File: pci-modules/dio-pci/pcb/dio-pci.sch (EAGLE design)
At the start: 132 parts, among them IC1 AZ1117CH-3.3, Q1 BSH103, Q2 BSH103, U1 4901, U3 ADN4663, U4 ADN4663, U5 ADN4664, U6 MEV3S1209SC, U7 4901

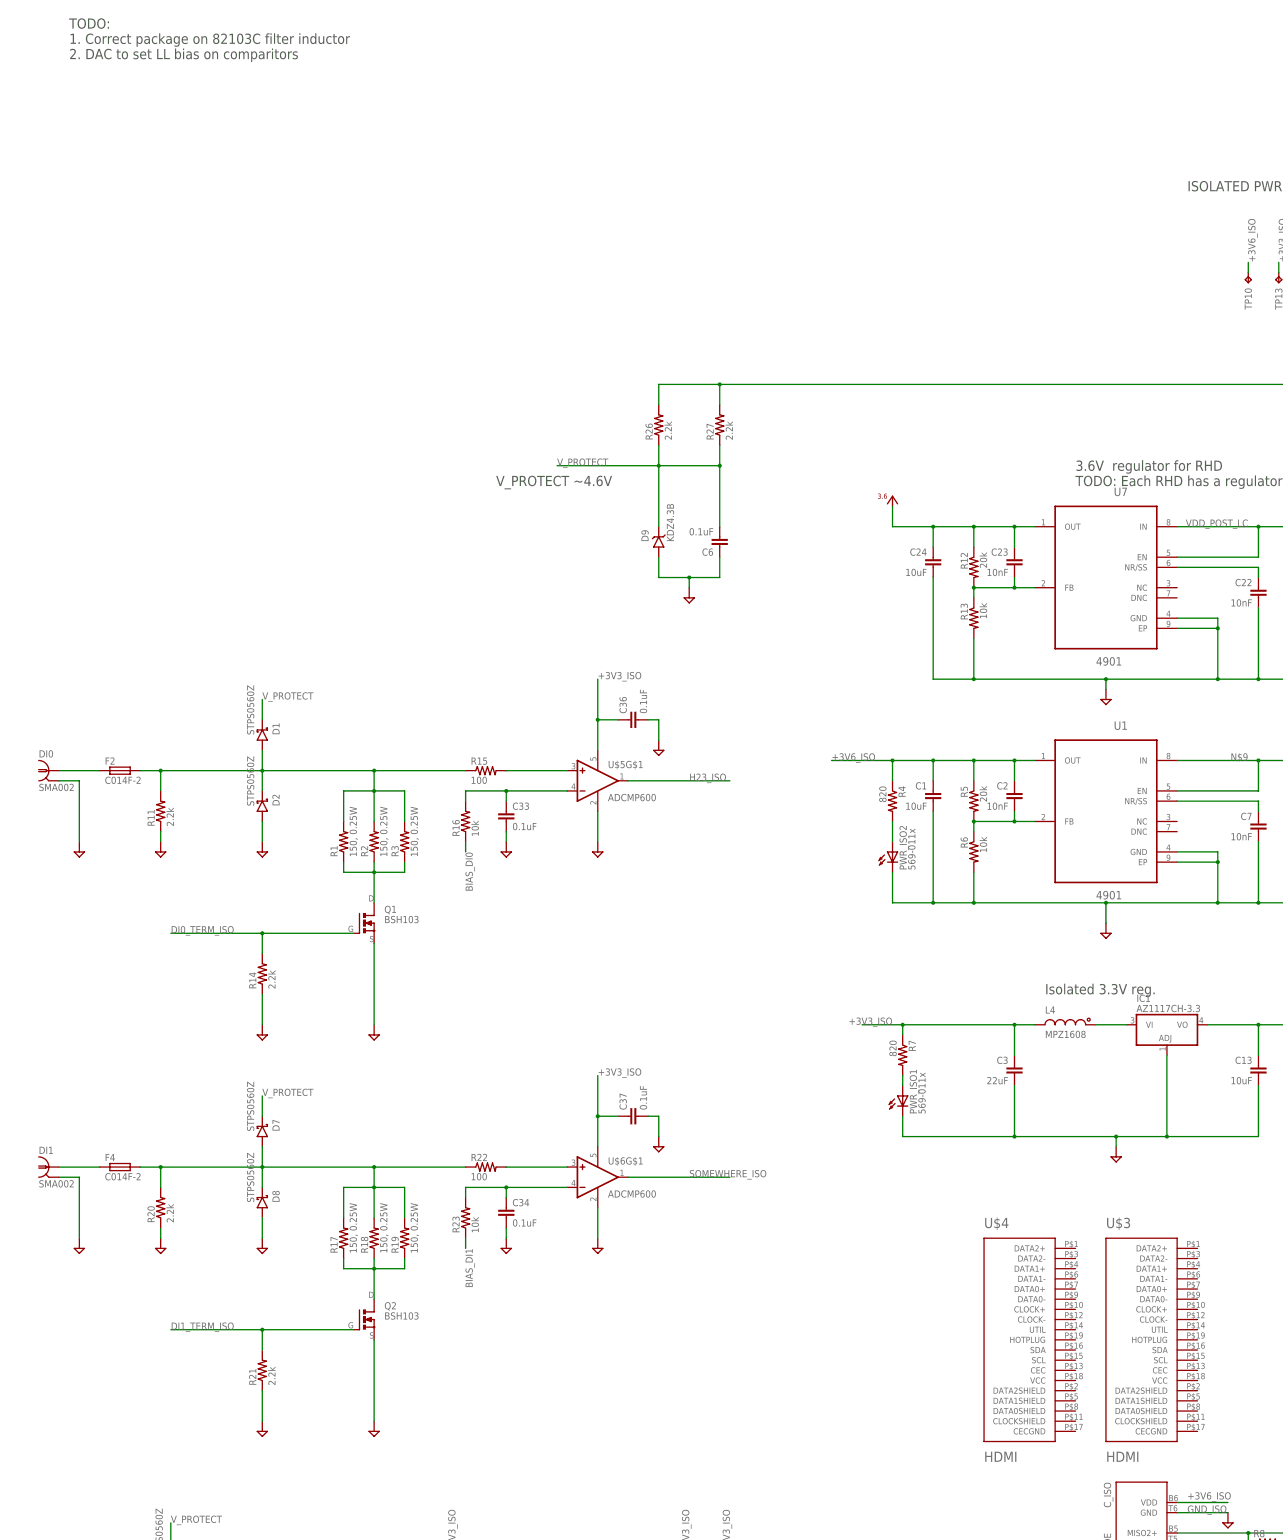
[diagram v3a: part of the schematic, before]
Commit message: Added some design ideas to dio-pci README.
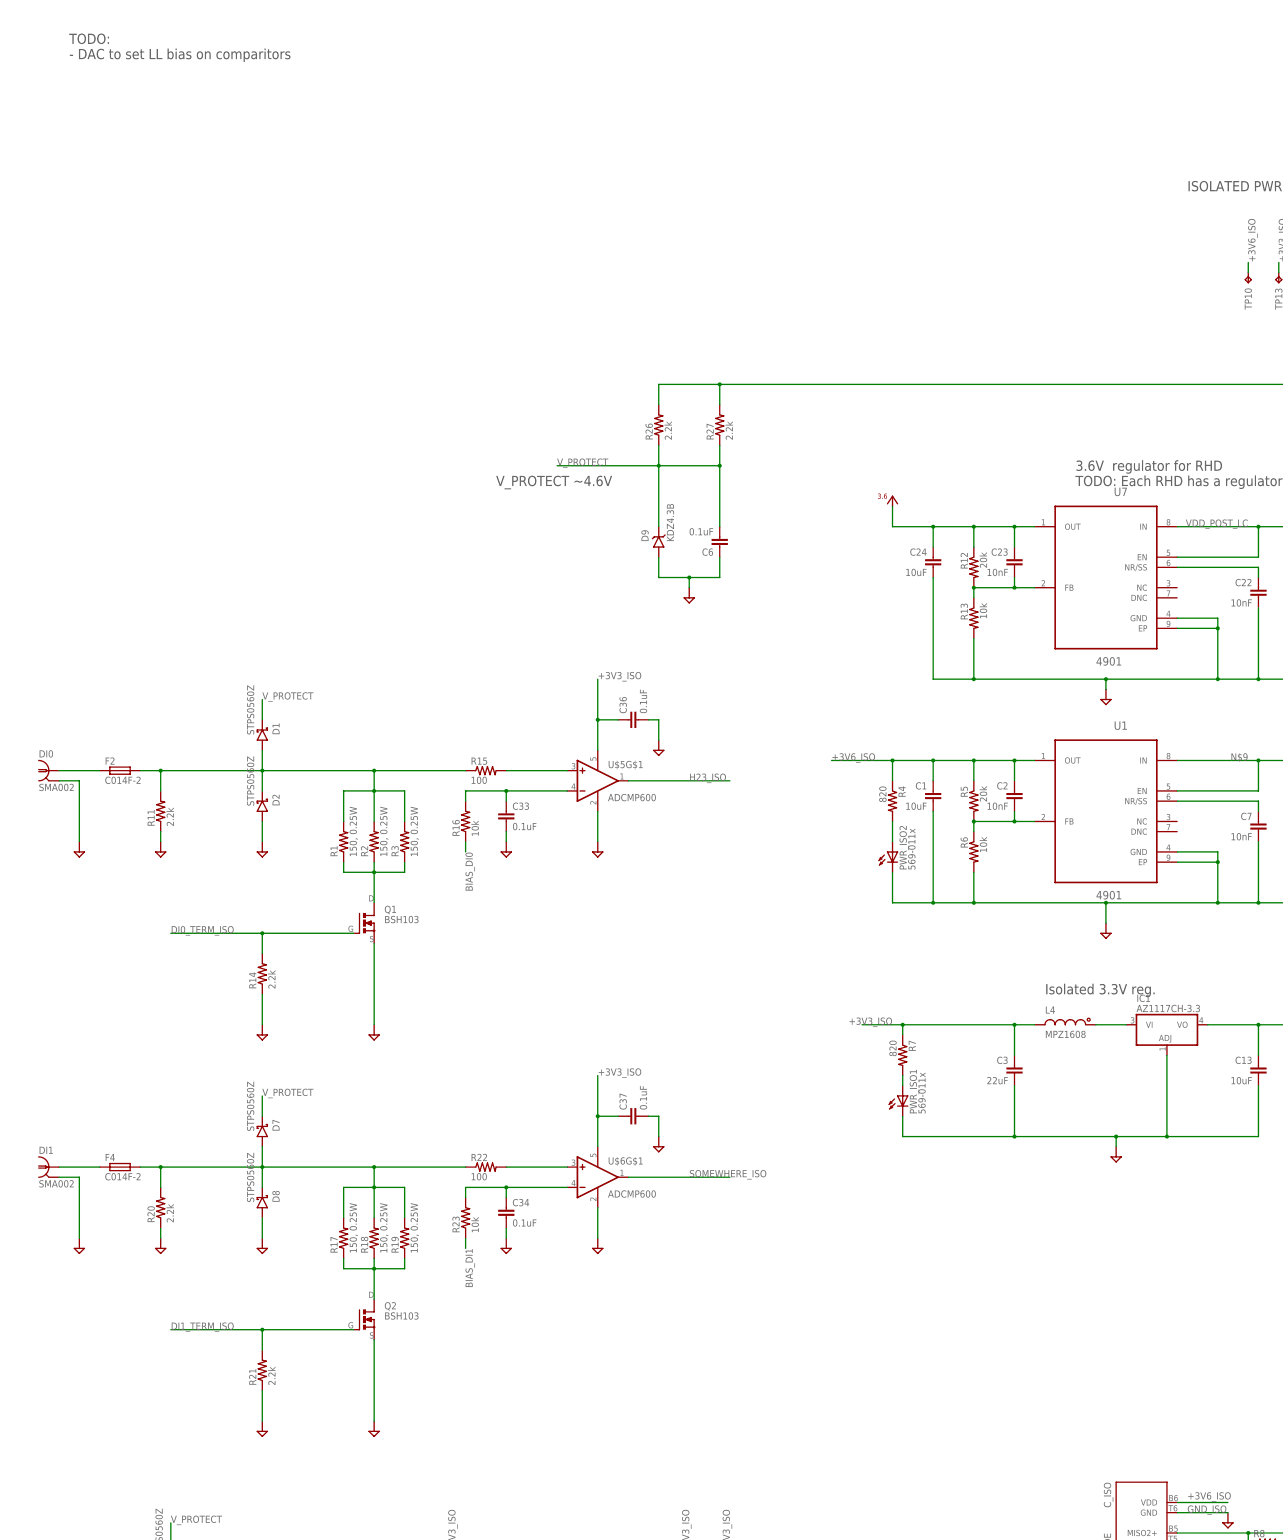
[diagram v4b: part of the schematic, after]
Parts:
- removed U$3, U$4: HDMI, jonnew:HDMI
- L5: device jonnew:L_1206 -> jonnew:L_1210
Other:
- note added: "TODO: - DAC to set LL bias on comparitors"
- note removed: "TODO: 1. Correct package on 82103C filter inductor 2. DAC to set LL bias on comparitors"
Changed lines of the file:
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@@
 <setting verticaltext="up"/>
 </settings>
-<grid distance="0.1" unitdist="inch" unit="inch" style="lines" multiple="1" display="yes" altdistance="0.01" altunitdist="inch" altunit="inch"/>
+<grid distance="0.1" unitdist="inch" unit="inch" style="lines" multiple="1" display="no" altdistance="0.01" altunitdist="inch" altunit="inch"/>
 <layers>
 <layer number="1" name="Top" color="4" fill="1" visible="no" active="no"/>
@@
 <layer number="91" name="Nets" color="2" fill="1" visible="yes" active="yes"/>
 <layer number="92" name="Busses" color="1" fill="1" visible="yes" active="yes"/>
-<layer number="93" name="Pins" color="2" fill="1" visible="no" active="yes"/>
+<layer number="93" name="Pins" color="2" fill="1" visible="yes" active="yes"/>
 <layer number="94" name="Symbols" color="4" fill="1" visible="yes" active="yes"/>
 <layer number="95" name="Names" color="7" fill="1" visible="yes" active="yes"/>
@@
 <layer number="97" name="Info" color="9" fill="1" visible="yes" active="yes"/>
 <layer number="98" name="Guide" color="6" fill="1" visible="yes" active="yes"/>
-<layer number="99" name="SpiceOrder" color="5" fill="1" visible="no" active="yes"/>
+<layer number="99" name="SpiceOrder" color="5" fill="1" visible="yes" active="yes"/>
 <layer number="100" name="help" color="7" fill="1" visible="yes" active="yes"/>
 <layer number="101" name="DOC" color="7" fill="1" visible="yes" active="yes"/>
 <layer number="102" name="bot_pads" color="7" fill="1" visible="yes" active="yes"/>
-<layer number="103" name="fp3" color="7" fill="1" visible="no" active="yes"/>
+<layer number="103" name="fp3" color="7" fill="1" visible="yes" active="yes"/>
 <layer number="104" name="S_DOKU" color="7" fill="1" visible="yes" active="yes"/>
 <layer number="105" name="Beschreib" color="9" fill="1" visible="yes" active="yes"/>
 <layer number="106" name="BGA-Top" color="4" fill="1" visible="yes" active="yes"/>
 <layer number="107" name="BD-Top" color="5" fill="1" visible="yes" active="yes"/>
-<layer number="108" name="fp8" color="7" fill="1" visible="no" active="yes"/>
-<layer number="109" name="fp9" color="7" fill="1" visible="no" active="yes"/>
-<layer number="110" name="fp0" color="7" fill="1" visible="no" active="yes"/>
+<layer number="108" name="fp8" color="7" fill="1" visible="yes" active="yes"/>
+<layer number="109" name="fp9" color="7" fill="1" visible="yes" active="yes"/>
+<layer number="110" name="fp0" color="7" fill="1" visible="yes" active="yes"/>
 <layer number="111" name="LPC17xx" color="7" fill="1" visible="yes" active="yes"/>
 <layer number="112" name="tSilk" color="7" fill="1" visible="yes" active="yes"/>
@@
 <layer number="121" name="_tsilk" color="7" fill="1" visible="yes" active="yes"/>
 <layer number="122" name="_bsilk" color="7" fill="1" visible="yes" active="yes"/>
-<layer number="123" name="tTestmark" color="7" fill="1" visible="no" active="yes"/>
-<layer number="124" name="bTestmark" color="7" fill="1" visible="no" active="yes"/>
+<layer number="123" name="tTestmark" color="7" fill="1" visible="yes" active="yes"/>
+<layer number="124" name="bTestmark" color="7" fill="1" visible="yes" active="yes"/>
 <layer number="125" name="_tNames" color="7" fill="1" visible="yes" active="yes"/>
 <layer number="126" name="_bNames" color="7" fill="1" visible="yes" active="yes"/>
 <layer number="127" name="_tValues" color="7" fill="1" visible="yes" active="yes"/>
 <layer number="128" name="_bValues" color="7" fill="1" visible="yes" active="yes"/>
-<layer number="131" name="tAdjust" color="7" fill="1" visible="no" active="yes"/>
-<layer number="132" name="bAdjust" color="7" fill="1" visible="no" active="yes"/>
+<layer number="131" name="tAdjust" color="7" fill="1" visible="yes" active="yes"/>
+<layer number="132" name="bAdjust" color="7" fill="1" visible="yes" active="yes"/>
 <layer number="144" name="Drill_legend" color="7" fill="1" visible="yes" active="yes"/>
-<layer number="150" name="Notes" color="7" fill="1" visible="no" active="yes"/>
+<layer number="150" name="Notes" color="7" fill="1" visible="yes" active="yes"/>
 <layer number="151" name="HeatSink" color="7" fill="1" visible="yes" active="yes"/>
 <layer number="152" name="_bDocu" color="7" fill="1" visible="yes" active="yes"/>
@@
 <layer number="200" name="200bmp" color="1" fill="10" visible="yes" active="yes"/>
 <layer number="201" name="201bmp" color="2" fill="10" visible="yes" active="yes"/>
-<layer number="202" name="202bmp" color="3" fill="10" visible="no" active="yes"/>
-<layer number="203" name="203bmp" color="4" fill="10" visible="no" active="yes"/>
-<layer number="204" name="204bmp" color="5" fill="10" visible="no" active="yes"/>
-<layer number="205" name="205bmp" color="6" fill="10" visible="no" active="yes"/>
-<layer number="206" name="206bmp" color="7" fill="10" visible="no" active="yes"/>
-<layer number="207" name="207bmp" color="8" fill="10" visible="no" active="yes"/>
-<layer number="208" name="208bmp" color="9" fill="10" visible="no" active="yes"/>
-<layer number="209" name="209bmp" color="10" fill="10" visible="no" active="yes"/>
-<layer number="210" name="210bmp" color="11" fill="10" visible="no" active="yes"/>
-<layer number="211" name="211bmp" color="12" fill="10" visible="no" active="yes"/>
-<layer number="212" name="212bmp" color="13" fill="10" visible="no" active="yes"/>
-<layer number="213" name="213bmp" color="14" fill="10" visible="no" active="yes"/>
-<layer number="214" name="214bmp" color="15" fill="10" visible="no" active="yes"/>
-<layer number="215" name="215bmp" color="16" fill="10" visible="no" active="yes"/>
-<layer number="216" name="216bmp" color="17" fill="10" visible="no" active="yes"/>
+<layer number="202" name="202bmp" color="3" fill="10" visible="yes" active="yes"/>
+<layer number="203" name="203bmp" color="4" fill="10" visible="yes" active="yes"/>
+<layer number="204" name="204bmp" color="5" fill="10" visible="yes" active="yes"/>
+<layer number="205" name="205bmp" color="6" fill="10" visible="yes" active="yes"/>
+<layer number="206" name="206bmp" color="7" fill="10" visible="yes" active="yes"/>
+<layer number="207" name="207bmp" color="8" fill="10" visible="yes" active="yes"/>
+<layer number="208" name="208bmp" color="9" fill="10" visible="yes" active="yes"/>
+<layer number="209" name="209bmp" color="10" fill="10" visible="yes" active="yes"/>
+<layer number="210" name="210bmp" color="11" fill="10" visible="yes" active="yes"/>
+<layer number="211" name="211bmp" color="12" fill="10" visible="yes" active="yes"/>
+<layer number="212" name="212bmp" color="13" fill="10" visible="yes" active="yes"/>
+<layer number="213" name="213bmp" color="14" fill="10" visible="yes" active="yes"/>
+<layer number="214" name="214bmp" color="15" fill="10" visible="yes" active="yes"/>
+<layer number="215" name="215bmp" color="16" fill="10" visible="yes" active="yes"/>
+<layer number="216" name="216bmp" color="17" fill="10" visible="yes" active="yes"/>
 <layer number="217" name="217bmp" color="18" fill="1" visible="no" active="no"/>
 <layer number="218" name="218bmp" color="19" fill="1" visible="no" active="no"/>
@@
 <part name="TP15" library="jonnew" deviceset="TP" device="TP06R" value="+5V0"/>
 <part name="U$2" library="jonnew" deviceset="PCI-MECH" device="_STD-H_HALF-W"/>
-<part name="U$3" library="jonnew" deviceset="HDMI" device=""/>
 <part name="GND1" library="jonnew" deviceset="GND_ISO" device=""/>
-<part name="U$4" library="jonnew" deviceset="HDMI" device=""/>
 <part name="F1" library="jonnew" deviceset="FUSE" device="_1812" value="C014F-2"/>
 <part name="F2" library="jonnew" deviceset="FUSE" device="_1812" value="C014F-2"/>
@@
 <part name="L3" library="jonnew" deviceset="L" device="_0603" value="MPZ1608"/>
 <part name="L4" library="jonnew" deviceset="L" device="_0603" value="MPZ1608"/>
-<part name="L5" library="jonnew" deviceset="L" device="_1206" value=" 82103C"/>
+<part name="L5" library="jonnew" deviceset="L" device="_1210" value=" 82103C"/>
 <part name="R26" library="jonnew" deviceset="R" device="_0603" value="2.2k"/>
 <part name="R27" library="jonnew" deviceset="R" device="_0603" value="2.2k"/>
@@
 <text x="599.44" y="208.28" size="2.54" layer="97">PCI ADD IN CARD</text>
 <text x="22.86" y="541.02" size="2.54" layer="97">TODO:
-1. Correct package on 82103C filter inductor
-2. DAC to set LL bias on comparitors</text>
+- DAC to set LL bias on comparitors</text>
 <text x="129.54" y="434.34" size="2.54" layer="97">V_PROTECT ~4.6V</text>
 </plain>
@@
 <instance part="TP15" gate="G$1" x="332.74" y="485.14" rot="R180"/>
 <instance part="U$2" gate="G$1" x="596.9" y="185.42"/>
-<instance part="U$3" gate="G$1" x="299.72" y="223.52"/>
 <instance part="GND1" gate="G$1" x="281.94" y="383.54"/>
-<instance part="U$4" gate="G$1" x="269.24" y="223.52"/>
 <instance part="F1" gate="G$1" x="35.56" y="157.48"/>
 <instance part="F2" gate="G$1" x="35.56" y="363.22"/>
